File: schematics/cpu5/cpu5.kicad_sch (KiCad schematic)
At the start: 52 parts, among them J1 Conn_01x12, J2 Conn_01x03, J3 Conn_01x40, J4 Conn_01x05, U1 74LS161, U10 74LS574, U11 74LS574, U12 74LS08, U13 74LS138, U14 74LS138, U15 74LS138, U16 74LS138, U17 74LS138, U18 74LS138, U19 74LS138, U2 74LS161, U20 74LS138, U21 74LS08, U22 74LS04, U23 74LS86, U24 74LS32, U25 74LS86, U26 74LS08, U27 74LS138, U28 74LS04, U29 74LS32, U30 74LS32, U31 74LS08, U32 74LS32, U33 74LS32, U34 74LS74, U35 74LS541, U36 74LS541, U4 74LS04, U42 74LS541, U5 74LS08, U6 74LS32, U7 74LS08, U8 74LS32, U82 74LS541, U9 74LS32

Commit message: os + ints work, ZF issue
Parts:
- added DbgConn2, IRQ_conn1: Conn_01x04, Connector_PinHeader_1.00mm:PinHeader_1x04_P1.00mm_Vertical, symbol Connector_Generic:Conn_01x04
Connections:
- net ADDR0: now also CONN_ADDRESS1.1 (Pin_1), U35.18 (Y0), U36.18 (Y0)
- net ADDR1: now also CONN_ADDRESS1.2 (Pin_2), U35.17 (Y1), U36.17 (Y1)
- net ADDR10: now also CONN_ADDRESS1.11 (Pin_11), U42.16 (Y2)
- net ADDR11: now also CONN_ADDRESS1.12 (Pin_12), U42.15 (Y3)
- net ADDR12: now also CONN_ADDRESS1.13 (Pin_13), U42.14 (Y4)
- net ADDR13: now also CONN_ADDRESS1.14 (Pin_14), U42.13 (Y5)
- net ADDR14: now also CONN_ADDRESS1.15 (Pin_15), U42.12 (Y6)
- net ADDR15: now also CONN_ADDRESS1.16 (Pin_16), U42.11 (Y7)
- net ADDR2: now also CONN_ADDRESS1.3 (Pin_3), U35.16 (Y2), U36.16 (Y2)
- net ADDR3: now also CONN_ADDRESS1.4 (Pin_4), U35.15 (Y3), U36.15 (Y3)
- net ADDR4: now also CONN_ADDRESS1.5 (Pin_5), U35.14 (Y4), U36.14 (Y4)
- net ADDR5: now also CONN_ADDRESS1.6 (Pin_6), U35.13 (Y5), U36.13 (Y5)
- net ADDR6: now also CONN_ADDRESS1.7 (Pin_7), U35.12 (Y6), U36.12 (Y6)
- net ADDR7: now also CONN_ADDRESS1.8 (Pin_8), U35.11 (Y7), U36.11 (Y7)
- net ADDR8: now also CONN_ADDRESS1.9 (Pin_9), U42.18 (Y0)
- net ADDR9: now also CONN_ADDRESS1.10 (Pin_10), U42.17 (Y1)
- net GND: no longer U8.10 (B3), U8.13 (B4), U8.2 (B1), U8.5 (B2), U9.10 (B3), U9.13 (B4), U9.2 (B1), U9.5 (B2)
- net ei: now also U28.2 (Y0); no longer U15.10 (Y5)
- net at U28.1 (A0): now also U15.10 (Y5)
- net seq_reset renamed SAMPLE_IRQ
- net SAMPLE_IRQ: now also IRQ_conn1.2 (Pin_2)
- new net DBG_INT_EN: DbgConn2.1 (Pin_1)
- new net DBG_PRE_INT1: DbgConn2.2 (Pin_2)
- new net DBG_PRE_INT2: DbgConn2.3 (Pin_3)
- new net DBG_PRE_INT3: DbgConn2.4 (Pin_4)
- new net IRQ: IRQ_conn1.1 (Pin_1), U8.10 (B3), U8.13 (B4), U8.2 (B1), U8.5 (B2), U9.10 (B3), U9.13 (B4), U9.2 (B1), U9.5 (B2)
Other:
- added sheet Interrupts (interrupts.kicad_sch)
- moved on the sheet: U28A

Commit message: Multithread + paging!
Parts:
- added J5: Conn_01x03, Connector_PinHeader_2.54mm:PinHeader_1x03_P2.54mm_Vertical, symbol Connector_Generic:Conn_01x03
- MCODE_HIGH1, MCODE_LOW1: VerilogInclude icechips/roms.v -> icechips/memory.v
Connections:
- net SELa renamed SELa_PGdis
- net dbg_mcode0 renamed mcode0
- net dbg_mcode1 renamed mcode1
- net dbg_mcode10: no longer names the net of U11.17 (Y2), U21.4 (A2)
- net dbg_mcode11: no longer names the net of U11.16 (Y3), U21.9 (A3)
- net dbg_mcode13: no longer names the net of U11.14 (Y5), U28.9 (A3)
- net dbg_mcode15: no longer names the net of U11.12 (Y7), U13.5 (Enable2_bar), U14.5 (Enable2_bar), U15.5 (Enable2_bar), U16.5 (Enable2_bar), U4.9 (A3)
- net dbg_mcode2: no longer names the net of U10.17 (Y2), U13.3 (A2), U14.3 (A2), U15.3 (A2), U16.3 (A2), U17.3 (A2), U18.3 (A2), U19.3 (A2), U20.3 (A2)
- net dbg_mcode3: no longer names the net of U10.16 (Y3), U13.6 (Enable3), U17.6 (Enable3)
- net dbg_mcode4: no longer names the net of U10.15 (Y4), U14.6 (Enable3), U18.6 (Enable3)
- net dbg_mcode5: no longer names the net of U10.14 (Y5), U12.1 (A1), U12.9 (A3)
- net dbg_mcode6: no longer names the net of U10.13 (Y6), U12.12 (A4), U12.4 (A2)
- net dbg_mcode7 renamed seq_reset_rq
- net dbg_mcode8: no longer names the net of U11.19 (Y0), U21.1 (A1)
- net dbg_mcode9: no longer names the net of U11.18 (Y1), U22.9 (A3)

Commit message: start faults
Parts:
- removed CONN_DATA1: Conn_01x08, Connector_PinHeader_2.54mm:PinHeader_1x08_P2.54mm_Vertical, symbol Connector_Generic:Conn_01x08
- added IR_BUF1: 74LS574, Package_DIP:DIP-20_W7.62mm, symbol 7400_ice:74LS574
- added U122: 74LS541, Package_DIP:DIP-20_W7.62mm, symbol 7400_ice:74LS541
- added U124: 74LS32, Package_DIP:DIP-14_W7.62mm, symbol 7400_ice:74LS32
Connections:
- net +5V: now also IR_BUF1.1 (OE_bar), IR_BUF1.20 (VCC), U122.20 (VCC)
- net GND: now also IR_BUF1.10 (GND), U122.1 (OE1_bar), U122.10 (GND), U122.19 (OE2_bar), U124.2 (B1)
- net IR0: now also IR_BUF1.2 (D0)
- net IR1: now also IR_BUF1.3 (D1)
- net IR2: now also IR_BUF1.4 (D2)
- net IR3: now also IR_BUF1.5 (D3)
- net IR4: now also IR_BUF1.6 (D4)
- net IR5: now also IR_BUF1.7 (D5)
- net IR6: now also IR_BUF1.8 (D6)
- net IR7: now also IR_BUF1.9 (D7)
- net IRi: now also IR1.11 (CLK); no longer U32.9 (A3)
- net SAMPLE_IRQ: now also U124.1 (A1); no longer U4.13 (A5)
- net init_ir: now also U32.9 (A3)
- net at U32.8 (Y3): no longer IR1.11 (CLK)
- net iIR0: no longer names the net of U8.3 (Y1)
- net iIR0: now also U122.2 (A0); no longer IR1.2 (D0)
- net iIR1: no longer names the net of IR1.3 (D1)
- net iIR1: now also IR_BUF1.18 (Y1), U122.17 (Y1); no longer U8.6 (Y2)
- net iIR2: no longer names the net of U8.8 (Y3)
- net iIR2: now also U122.4 (A2); no longer IR1.4 (D2)
- net iIR3: no longer names the net of IR1.5 (D3)
- net iIR3: now also IR_BUF1.16 (Y3), U122.15 (Y3); no longer U8.11 (Y4)
- net iIR4: no longer names the net of IR1.6 (D4)
- net iIR4: now also IR_BUF1.15 (Y4), U122.14 (Y4); no longer U9.3 (Y1)
- net iIR5: no longer names the net of U9.6 (Y2)
- net iIR5: now also U122.7 (A5); no longer IR1.7 (D5)
- net iIR6: no longer names the net of IR1.8 (D6)
- net iIR6: now also IR_BUF1.13 (Y6), U122.12 (Y6); no longer U9.8 (Y3)
- net iIR7: no longer names the net of U9.11 (Y4)
- net iIR7: now also U122.9 (A7); no longer IR1.9 (D7)
- new net: IR1.9 (D7), IR_BUF1.12 (Y7), U122.11 (Y7)
- new net: IR1.7 (D5), IR_BUF1.14 (Y5), U122.13 (Y5)
- new net: IR1.4 (D2), IR_BUF1.17 (Y2), U122.16 (Y2)
- new net: IR1.2 (D0), IR_BUF1.19 (Y0), U122.18 (Y0)
- new net: U122.3 (A1), U8.6 (Y2)
- new net: U122.5 (A3), U8.11 (Y4)
- new net: U122.6 (A4), U9.3 (Y1)
- new net: U122.8 (A6), U9.8 (Y3)
- new net: U124.3 (Y1), U4.13 (A5)
- new net MMU_FAULT: IR_BUF1.11 (CLK)
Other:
- moved on the sheet: CONN_ADDRESS1, DbgConn2, INTERNAL_ADDRESS_CONN1, INTERNAL_DATA_CONN1, INTERNAL_DATA_CONN2, IR1, IRQ_conn1, J1, J2, J3, J4, J5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

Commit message: faults seem to work
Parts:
- removed Jdbg1: Conn_01x12, Connector_PinHeader_2.54mm:PinHeader_1x12_P2.54mm_Vertical, symbol Connector_Generic:Conn_01x12
- added U125: 74LS32, Package_DIP:DIP-14_W7.62mm, symbol 7400_ice:74LS32
- added U126: 74LS04, Package_DIP:DIP-14_W7.62mm, symbol 7400_ice:74LS04
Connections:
- net +5V: now also U126.14 (VCC)
- net GND: now also U126.7 (GND)
- net IRQ: now also U31.9 (A3)
- net IRi: now also U32.10 (B3); no longer IR1.11 (CLK)
- net SAMPLE_IRQ: now also U7.3 (Y1); no longer U7.6 (Y2)
- net init_ir: no longer U32.10 (B3), U32.9 (A3)
- net mpc0: now also U125.12 (A4)
- net mpc1: now also U125.13 (B4)
- net mpc2: now also U125.1 (A1)
- net mpc3: now also U125.2 (B1)
- net phase_mread: now also U124.13 (B4), U124.8 (Y3); no longer U7.11 (Y4)
- net phase_write: now also U5.9 (A3), U7.6 (Y2); no longer U7.3 (Y1)
- net at U7.9 (A3): now also U126.12 (Y5); no longer U5.3 (Y1)
- net at U2.13 (Q1): now also U124.5 (B2), U5.5 (B2); no longer U5.2 (B1)
- net at U124.11 (Y4): now also U4.3 (A1)
- net at U124.12 (A4): now also U124.6 (Y2), U125.9 (A3)
- net at U4.1 (A0): now also U125.8 (Y3)
- net at U4.2 (Y0): now also U5.1 (A1)
- net at U124.4 (A2): now also U2.14 (Q0), U5.4 (A2)
- net at U32.8 (Y3): now also IR1.11 (CLK)
- net at U124.10 (B3): now also U2.11 (Q3), U7.5 (B2), U125.10 (B3)
- net at U124.9 (A3): now also U2.12 (Q2), U5.2 (B1), U7.4 (A2)
- net cword_en renamed cword_clk
- net cword_clk: now also U5.3 (Y1); no longer U5.8 (Y3)
- net seq_reset_rq: no longer names the net of U10.12 (Y7)
- net seq_reset_rq: now also U7.2 (B1); no longer U7.5 (B2)
- new net: U125.3 (Y1), U125.5 (B2)
- new net: U125.11 (Y4), U125.4 (A2)
- new net: U125.6 (Y2), U126.13 (A5)
- new net: U5.8 (Y3), U7.1 (A1)
- new net: U5.10 (B3), U5.6 (Y2)
- new net start_instr: U32.9 (A3), U7.8 (Y3)
- new net start_phase: U4.4 (Y1), U7.10 (B3)
- now unconnected: U7.12 (A4), U7.13 (B4)
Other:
- moved on the sheet: U124B, U124C, U124D, U31C, U32C, U4A, U4B, U5A, U5B, U5C, U7A, U7B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

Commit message: Page faults work
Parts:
- added IR_BUF2: 74LS574, Package_DIP:DIP-20_W7.62mm, symbol 7400_ice:74LS574
- added U132: 74LS541, Package_DIP:DIP-20_W7.62mm, symbol 7400_ice:74LS541
- added U133, U134: 74LS32, Package_DIP:DIP-14_W7.62mm, symbol 7400_ice:74LS32
- added U135: 74LS08, Package_DIP:DIP-14_W7.62mm, symbol 7400_ice:74LS08
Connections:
- net +5V: now also IR_BUF2.20 (VCC), U132.20 (VCC), U133.14 (VCC), U134.14 (VCC), U135.7 (GND); no longer IR_BUF1.1 (OE_bar)
- net FAULT: now also U133.10 (B3), U133.13 (B4), U133.2 (B1), U133.5 (B2), U134.10 (B3), U134.13 (B4), U134.2 (B1), U134.5 (B2), U135.2 (B1)
- net GND: now also U13.5 (Enable2_bar), U14.5 (Enable2_bar), U15.5 (Enable2_bar), U16.5 (Enable2_bar), U17.5 (Enable2_bar), U18.5 (Enable2_bar), U19.5 (Enable2_bar), U20.5 (Enable2_bar), IR_BUF2.10 (GND), IR_BUF2.2 (D0), IR_BUF2.3 (D1), IR_BUF2.4 (D2), IR_BUF2.5 (D3), U132.10 (GND), U132.19 (OE2_bar), U132.2 (A0), U132.3 (A1), U132.4 (A2), U132.5 (A3), U132.6 (A4), U132.7 (A5), U132.8 (A6), U132.9 (A7), U133.7 (GND), U134.7 (GND), U135.14 (VCC); no longer U1.3 (D0), U1.4 (D1), U1.5 (D2), U1.6 (D3), U122.1 (OE1_bar), U124.2 (B1), U2.3 (D0), U2.4 (D1), U2.5 (D2), U2.6 (D3)
- net SAMPLE_IRQ: now also U124.3 (Y1), U4.13 (A5); no longer U124.1 (A1), U24.12 (A4), U7.3 (Y1)
- net mpc0: now also IR_BUF2.6 (D4)
- net mpc1: now also IR_BUF2.7 (D5)
- net mpc2: now also IR_BUF2.8 (D6)
- net mpc3: now also IR_BUF2.9 (D7)
- net start_phase: now also U7.13 (B4)
- net mcode6: now reaches U10.13 (Y6), U12.12 (A4), U12.4 (A2)
- net at U9.6 (Y2): now also U134.4 (A2); no longer U122.7 (A5)
- net at U9.11 (Y4): now also U134.12 (A4); no longer U122.9 (A7)
- net at U8.3 (Y1): now also U133.1 (A1); no longer U122.2 (A0)
- net at U7.11 (Y4): now also U135.12 (A4)
- net at U7.12 (A4): now also U126.10 (Y4)
- net mcode2: now reaches U10.17 (Y2), U13.3 (A2), U14.3 (A2), U15.3 (A2), U16.3 (A2), U17.3 (A2), U18.3 (A2), U19.3 (A2), U20.3 (A2)
- net at U8.8 (Y3): now also U133.9 (A3); no longer U122.4 (A2)
- net preIR7: now reaches IR1.9 (D7), IR_BUF1.12 (Y7), U122.11 (Y7)
- net preIR6: now reaches IR1.8 (D6), IR_BUF1.13 (Y6), U122.12 (Y6)
- net preIR5: now reaches IR1.7 (D5), IR_BUF1.14 (Y5), U122.13 (Y5)
- net preIR4: now reaches IR1.6 (D4), IR_BUF1.15 (Y4), U122.14 (Y4)
- net preIR3: now reaches IR1.5 (D3), IR_BUF1.16 (Y3), U122.15 (Y3)
- net preIR2: now reaches IR1.4 (D2), IR_BUF1.17 (Y2), U122.16 (Y2)
- net preIR1: now reaches IR1.3 (D1), IR_BUF1.18 (Y1), U122.17 (Y1)
- net preIR0: now reaches IR1.2 (D0), IR_BUF1.19 (Y0), U122.18 (Y0)
- net at U8.6 (Y2): now also U133.4 (A2); no longer U122.3 (A1)
- net at U122.5 (A3): now also U133.11 (Y4); no longer U8.11 (Y4)
- net at U122.6 (A4): now also U134.3 (Y1); no longer U9.3 (Y1)
- net at U122.8 (A6): now also U134.8 (Y3); no longer U9.8 (Y3)
- net mcode3: now reaches U10.16 (Y3), U13.6 (Enable3), U17.6 (Enable3)
- net mcode5: now reaches U10.14 (Y5), U12.1 (A1), U12.9 (A3)
- net mcode4: now reaches U10.15 (Y4), U14.6 (Enable3), U18.6 (Enable3)
- net end_phase: now reaches U5.8 (Y3), U7.1 (A1)
- net end_phase: now also U135.1 (A1)
- net mcode7: now reaches U10.12 (Y7), U7.2 (B1)
- net FAULT_PENDING: now reaches U126.11 (A4)
- net MMU_FAULT renamed SAVE_FAULT
- net SAVE_FAULT: now also IR_BUF2.11 (CLK), U135.11 (Y4)
- new net: U135.13 (B4), U135.6 (Y2)
- new net: IR_BUF2.15 (Y4), U1.3 (D0), U132.14 (Y4)
- new net: IR_BUF2.14 (Y5), U1.4 (D1), U132.13 (Y5)
- new net: IR_BUF2.13 (Y6), U1.5 (D2), U132.12 (Y6)
- new net: IR_BUF2.12 (Y7), U1.6 (D3), U132.11 (Y7)
- new net: U122.3 (A1), U133.6 (Y2)
- new net: U122.2 (A0), U133.3 (Y1)
- new net: U122.4 (A2), U133.8 (Y3)
- new net: U122.7 (A5), U134.6 (Y2)
- new net: U122.9 (A7), U134.11 (Y4)
- new net: U133.12 (A4), U8.11 (Y4)
- new net: U124.2 (B1), U135.3 (Y1)
- new net: U134.1 (A1), U9.3 (Y1)
- new net: IR_BUF2.16 (Y3), U132.15 (Y3), U2.6 (D3)
- new net: IR_BUF2.17 (Y2), U132.16 (Y2), U2.5 (D2)
- new net: IR_BUF2.18 (Y1), U132.17 (Y1), U2.4 (D1)
- new net: IR_BUF2.19 (Y0), U132.18 (Y0), U2.3 (D0)
- new net: U134.9 (A3), U9.8 (Y3)
- new net LOAD_FAULT: U11.12 (Y7), U122.1 (OE1_bar), U132.1 (OE1_bar), U4.9 (A3)
- new net LOAD_FAULT_bar: IR_BUF1.1 (OE_bar), IR_BUF2.1 (OE_bar), U135.5 (B2), U4.8 (Y3)
- new net PGE: U135.4 (A2)
- new net seq_reset: U124.1 (A1), U24.12 (A4), U7.3 (Y1)
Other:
- note added: "Save OFF on FAULT!!! end_phase AND fault is incorrect!"
- moved on the sheet: IR_BUF1, J4, U122, U126A, U126B, U126C, U126D, U126E, U31C, U4D, U7D, U8A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

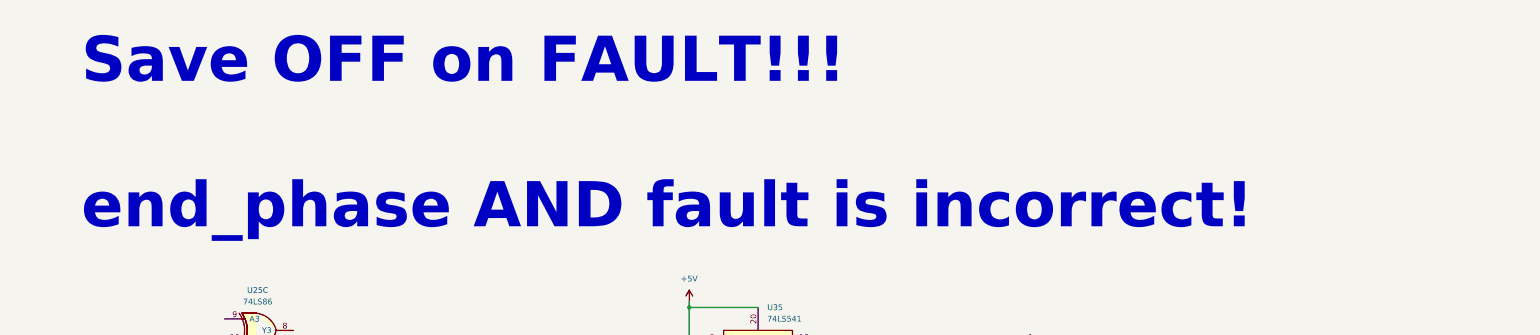
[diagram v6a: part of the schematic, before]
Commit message: user space works in lsim
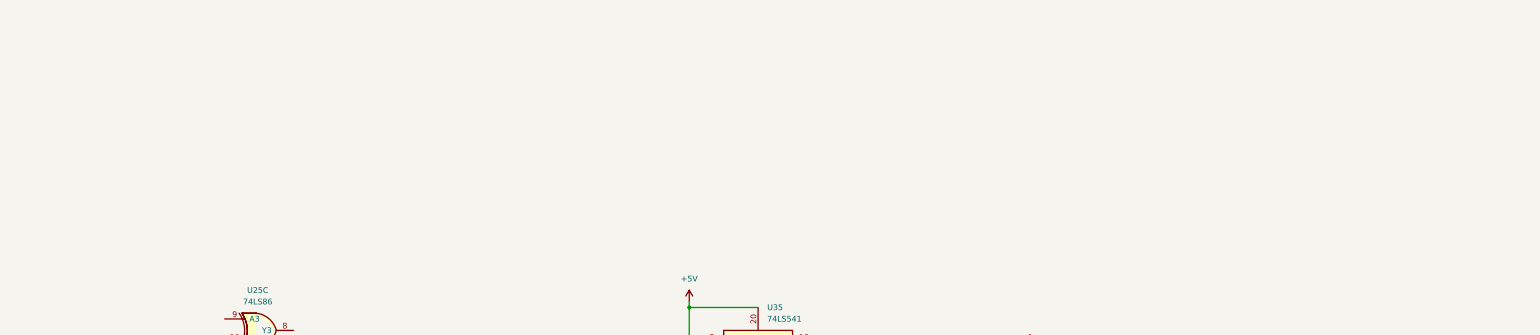
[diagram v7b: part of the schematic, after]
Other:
- note removed: "Save OFF on FAULT!!! end_phase AND fault is incorrect!"
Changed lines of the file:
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@@
     (stroke (width 0) (type default) (color 0 0 0 0))
-  )
-  (text "Save OFF on FAULT!!!\n\nend_phase AND fault is incorrect!"
-    (at 468.63 67.31 0)
-    (effects (font (size 10 10) bold) (justify left bottom))
   )
   (label "seq_reset" (at 386.08 180.34 0)
